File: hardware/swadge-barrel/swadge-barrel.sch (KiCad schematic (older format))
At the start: 44 parts, among them J1 USB_B_Micro, SW1 SW_SPDT, U1 AP1117-33, U2 ESP-13-WROOM-02D, U3 BUS_PCIexpress, U4 OLED_CONNECTOR, U5 QMA6981, U6 OLED_DISPLAY

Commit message: Updated descriptions to be more CSV friendly
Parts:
- U6: Notes Must be a single color, white. Must have SSD1306 driver. Mu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 -> Must be a single color; white. Must have SSD1306 driver. Mu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
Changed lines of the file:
@@
 F 6 "352" H 5850 6100 50  0001 C CNN "Cost100"
 F 7 "Y" H 5850 6100 50  0001 C CNN "Substitutable"
-F 8 "Must be a single color, white. Must have SSD1306 driver. Must have bottom pins, same as connector. 0.5mm pitch, like the connector" H 5850 6100 50  0001 C CNN "Notes"
+F 8 "Must be a single color; white. Must have SSD1306 driver. Must have bottom pins; same as connector. 0.5mm pitch; like the connector" H 5850 6100 50  0001 C CNN "Notes"
 	1    5850 6100
 	1    0    0    -1

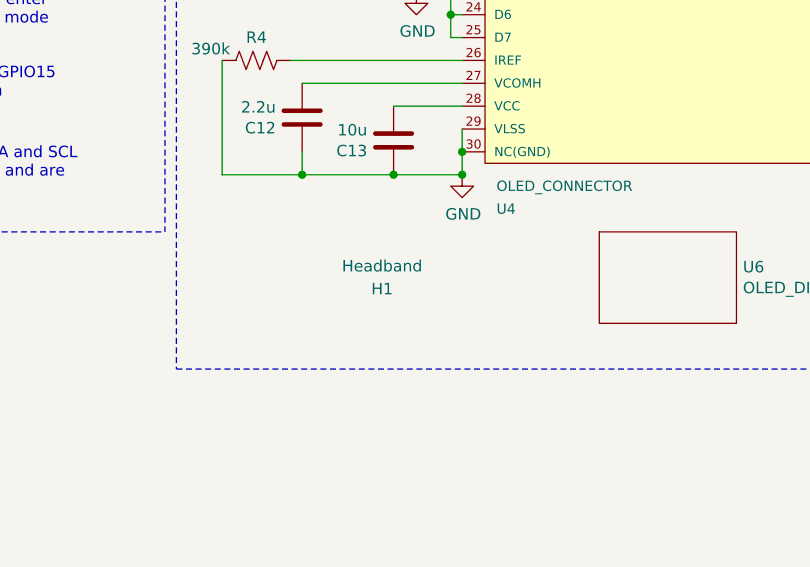
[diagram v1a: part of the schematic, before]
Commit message: Added H2 part designator
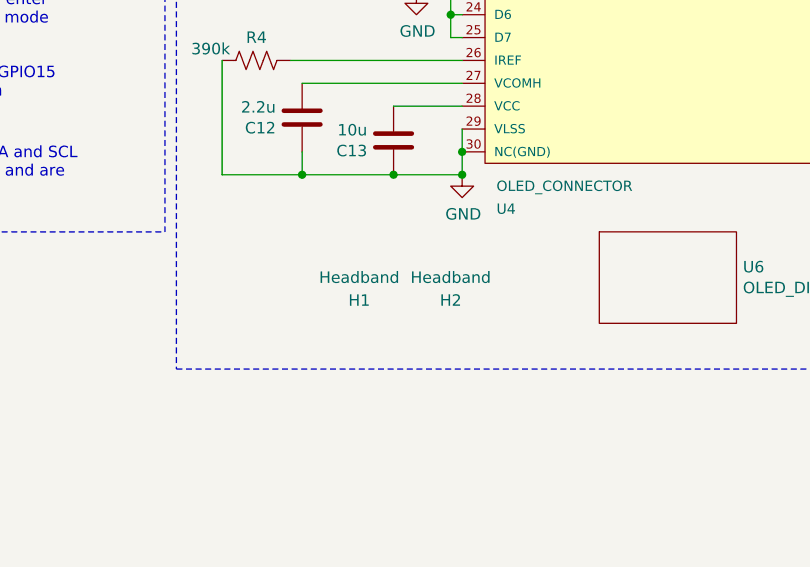
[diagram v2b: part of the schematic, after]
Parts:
- added H2: Headband, Swadge_Parts:NULL, symbol Swadge_Parts:Headband
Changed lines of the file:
@@
 L Swadge_Parts:Headband H1
 U 1 1 5D829692
-P 4600 6150
-F 0 "H1" H 4600 6150 50  0000 C CNN
-F 1 "Headband" H 4600 6250 50  0000 C CNN
-F 2 "Swadge_Parts:Headband" H 4600 6150 50  0001 C CNN
-F 3 "https://cdn.harwin.com/pdfs/M50-353.pdf" H 4600 6150 50  0001 C CNN
-F 4 "952-3598-ND" H 4600 6150 50  0001 C CNN "Digikey"
-F 5 "Use Swadge Headband PCB and two 2x1 male pin headers with 1.27mm spacing for assembly. Must attach OLED display before soldering headband. This is meant to protect the OLED's corners" H 4600 6150 50  0001 C CNN "Notes"
-F 6 "N" H 4600 6150 50  0001 C CNN "Substitutable"
-	1    4600 6150
+P 4500 6200
+F 0 "H1" H 4500 6200 50  0000 C CNN
+F 1 "Headband" H 4500 6300 50  0000 C CNN
+F 2 "Swadge_Parts:Headband" H 4500 6200 50  0001 C CNN
+F 3 "https://cdn.harwin.com/pdfs/M50-353.pdf" H 4500 6200 50  0001 C CNN
+F 4 "952-3598-ND" H 4500 6200 50  0001 C CNN "Digikey"
+F 5 "Use Swadge Headband PCB and two 2x1 male pin headers with 1.27mm spacing for assembly. Must attach OLED display before soldering headband. This is meant to protect the OLED's corners" H 4500 6200 50  0001 C CNN "Notes"
+F 6 "N" H 4500 6200 50  0001 C CNN "Substitutable"
+	1    4500 6200
 	1    0    0    -1
 $EndComp
@@
 Wire Notes Line
 	8550 2450 3700 2450
+$Comp
+L Swadge_Parts:Headband H2
+U 1 1 5DB44B4F
+P 4900 6200
+F 0 "H2" H 4900 6200 50  0000 C CNN
+F 1 "Headband" H 4900 6300 50  0000 C CNN
+F 2 "Swadge_Parts:NULL" H 4900 6200 50  0001 C CNN
+F 3 "https://cdn.harwin.com/pdfs/M50-353.pdf" H 4900 6200 50  0001 C CNN
+F 4 "952-3598-ND" H 4900 6200 50  0001 C CNN "Digikey"
+F 5 "This is the second 2x1 male pin header with 1.27mm spacing for assembly. " H 4900 6200 50  0001 C CNN "Notes"
+F 6 "N" H 4900 6200 50  0001 C CNN "Substitutable"
+	1    4900 6200
+	1    0    0    -1
+$EndComp
 $EndSCHEMATC

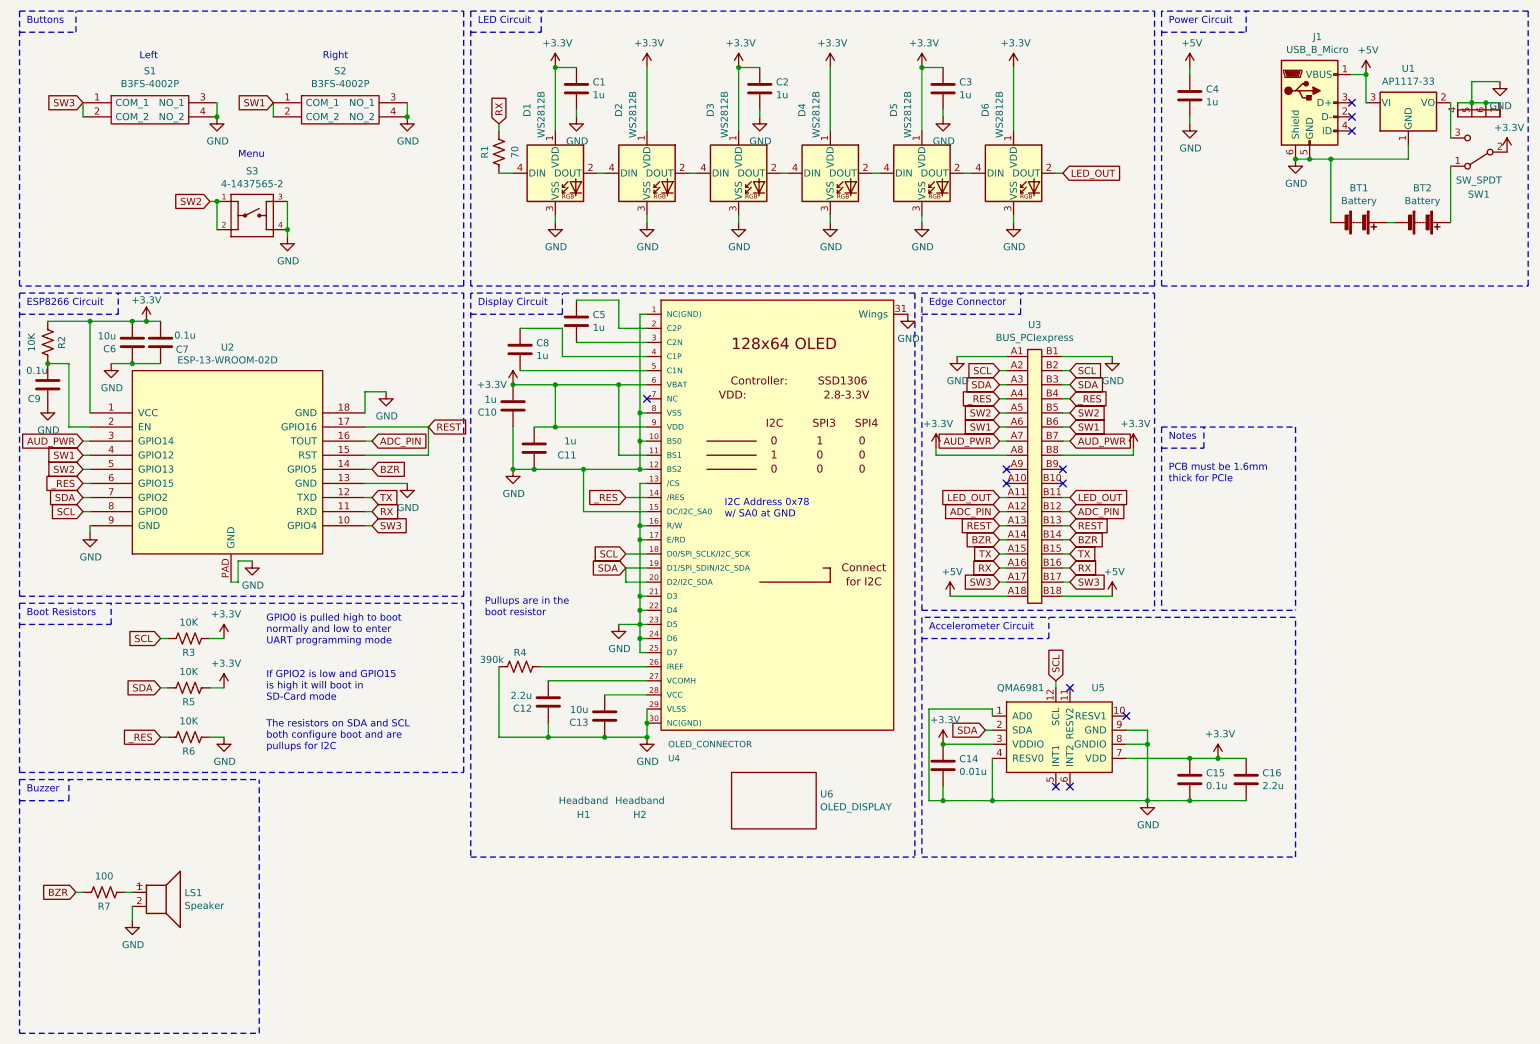
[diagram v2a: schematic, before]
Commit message: Modified barrel and programmer to use Swadge_Parts's power parts
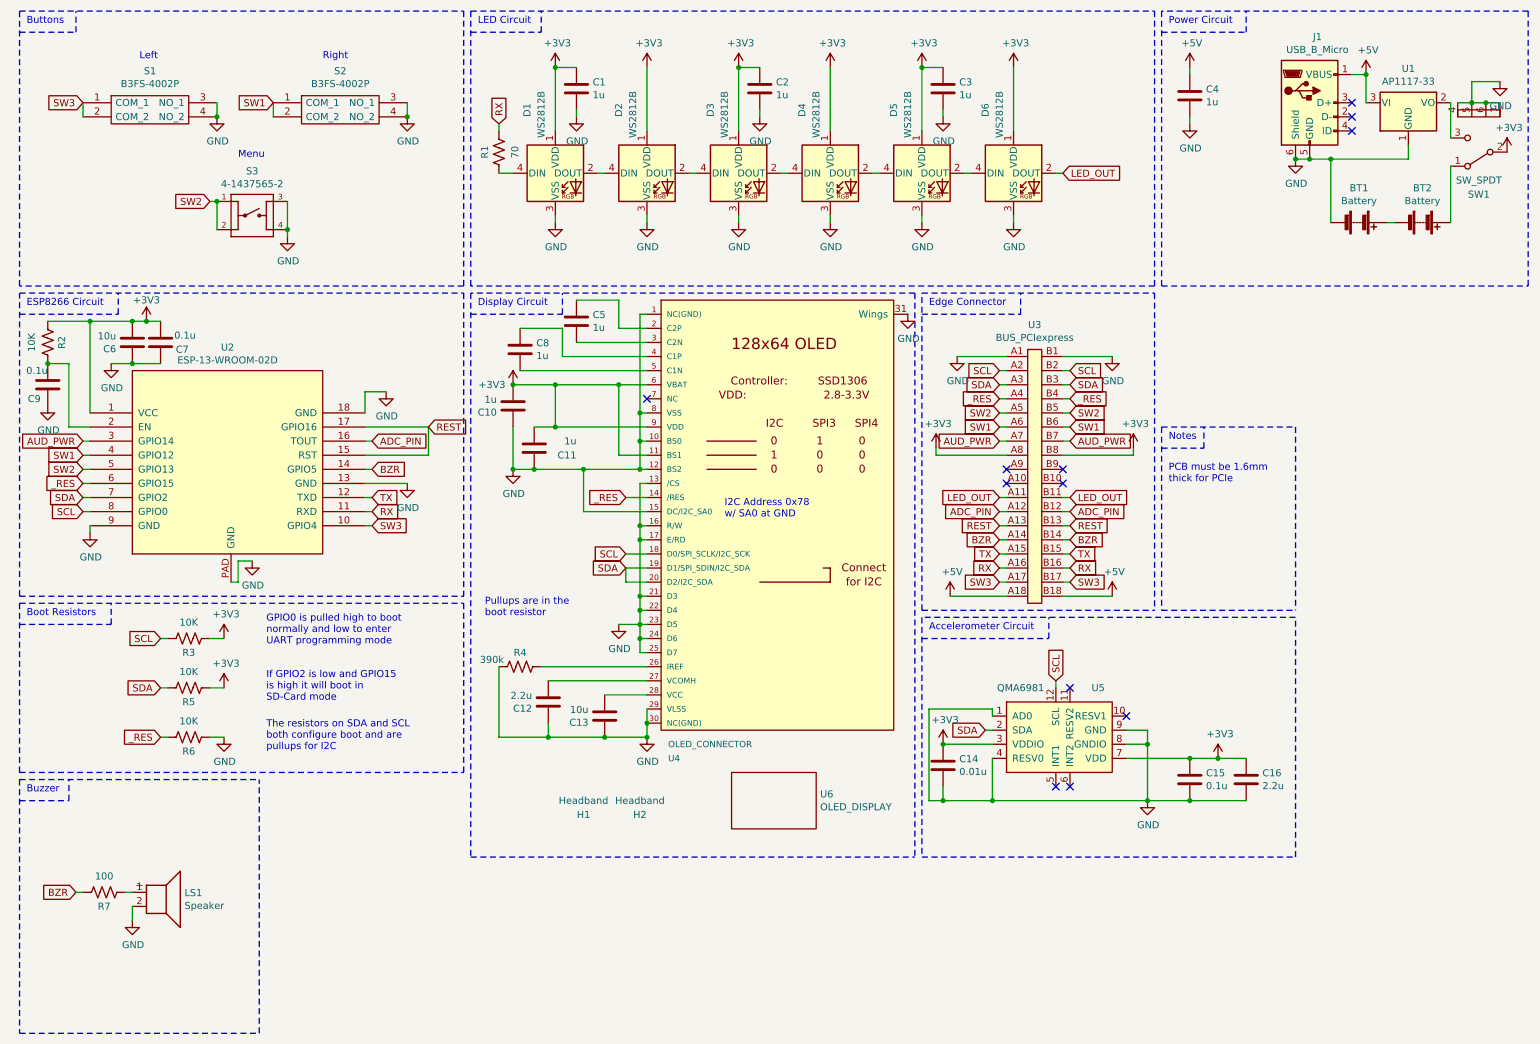
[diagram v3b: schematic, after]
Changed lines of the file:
@@
 $EndComp
 $Comp
-L power:+3.3V #PWR01
+L Swadge_Parts:+3V3 #PWR01
 U 1 1 5C3A6F38
 P 4300 900
 F 0 "#PWR01" H 4300 750 50  0001 C CNN
-F 1 "+3.3V" H 4315 1073 50  0000 C CNN
+F 1 "+3V3" H 4315 1073 50  0000 C CNN
 F 2 "" H 4300 900 50  0001 C CNN
 F 3 "" H 4300 900 50  0001 C CNN
@@
 $EndComp
 $Comp
-L power:GND #PWR012
+L Swadge_Parts:GND #PWR012
 U 1 1 5C3A6FCC
 P 4450 1250
@@
 Connection ~ 4300 900
 $Comp
-L power:GND #PWR018
+L Swadge_Parts:GND #PWR018
 U 1 1 5C3A78DA
 P 4300 2000
@@
 $EndComp
 $Comp
-L power:+3.3V #PWR02
+L Swadge_Parts:+3V3 #PWR02
 U 1 1 5C3A88AB
 P 4950 900
 F 0 "#PWR02" H 4950 750 50  0001 C CNN
-F 1 "+3.3V" H 4965 1073 50  0000 C CNN
+F 1 "+3V3" H 4965 1073 50  0000 C CNN
 F 2 "" H 4950 900 50  0001 C CNN
 F 3 "" H 4950 900 50  0001 C CNN
@@
 $EndComp
 $Comp
-L power:GND #PWR019
+L Swadge_Parts:GND #PWR019
 U 1 1 5C3A88C0
 P 4950 2000
@@
 $EndComp
 $Comp
-L power:+3.3V #PWR03
+L Swadge_Parts:+3V3 #PWR03
 U 1 1 5C3A91DF
 P 5600 900
 F 0 "#PWR03" H 5600 750 50  0001 C CNN
-F 1 "+3.3V" H 5615 1073 50  0000 C CNN
+F 1 "+3V3" H 5615 1073 50  0000 C CNN
 F 2 "" H 5600 900 50  0001 C CNN
 F 3 "" H 5600 900 50  0001 C CNN
@@
 $EndComp
 $Comp
-L power:GND #PWR013
+L Swadge_Parts:GND #PWR013
 U 1 1 5C3A91EB
 P 5750 1250
@@
 $EndComp
 $Comp
-L power:GND #PWR020
+L Swadge_Parts:GND #PWR020
 U 1 1 5C3A91F4
 P 5600 2000
@@
 $EndComp
 $Comp
-L power:+3.3V #PWR04
+L Swadge_Parts:+3V3 #PWR04
 U 1 1 5C3A9200
 P 6250 900
 F 0 "#PWR04" H 6250 750 50  0001 C CNN
-F 1 "+3.3V" H 6265 1073 50  0000 C CNN
+F 1 "+3V3" H 6265 1073 50  0000 C CNN
 F 2 "" H 6250 900 50  0001 C CNN
 F 3 "" H 6250 900 50  0001 C CNN
@@
 	6250 1350 6250 900
 $Comp
-L power:GND #PWR021
+L Swadge_Parts:GND #PWR021
 U 1 1 5C3A9215
 P 6250 2000
@@
 $EndComp
 $Comp
-L power:+3.3V #PWR05
+L Swadge_Parts:+3V3 #PWR05
 U 1 1 5C3A9722
 P 6900 900
 F 0 "#PWR05" H 6900 750 50  0001 C CNN
-F 1 "+3.3V" H 6915 1073 50  0000 C CNN
+F 1 "+3V3" H 6915 1073 50  0000 C CNN
 F 2 "" H 6900 900 50  0001 C CNN
 F 3 "" H 6900 900 50  0001 C CNN
@@
 $EndComp
 $Comp
-L power:GND #PWR014
+L Swadge_Parts:GND #PWR014
 U 1 1 5C3A972E
 P 7050 1250
@@
 Connection ~ 6900 900
 $Comp
-L power:GND #PWR022
+L Swadge_Parts:GND #PWR022
 U 1 1 5C3A9737
 P 6900 2000
@@
 $EndComp
 $Comp
-L power:+3.3V #PWR06
+L Swadge_Parts:+3V3 #PWR06
 U 1 1 5C3A9743
 P 7550 900
 F 0 "#PWR06" H 7550 750 50  0001 C CNN
-F 1 "+3.3V" H 7565 1073 50  0000 C CNN
+F 1 "+3V3" H 7565 1073 50  0000 C CNN
 F 2 "" H 7550 900 50  0001 C CNN
 F 3 "" H 7550 900 50  0001 C CNN
@@
 $EndComp
 $Comp
-L power:GND #PWR015
+L Swadge_Parts:GND #PWR015
 U 1 1 5C3A974F
 P 8800 1300
@@
 $EndComp
 $Comp
-L power:GND #PWR023
+L Swadge_Parts:GND #PWR023
 U 1 1 5C3A9758
 P 7550 2000
@@
 $EndComp
 $Comp
-L power:+3.3V #PWR042
+L Swadge_Parts:+3V3 #PWR042
 U 1 1 5C3B6E79
 P 1950 4950
 F 0 "#PWR042" H 1950 4800 50  0001 C CNN
-F 1 "+3.3V" H 1965 5123 50  0000 C CNN
+F 1 "+3V3" H 1965 5123 50  0000 C CNN
 F 2 "" H 1950 4950 50  0001 C CNN
 F 3 "" H 1950 4950 50  0001 C CNN
@@
 $EndComp
 $Comp
-L power:+3.3V #PWR043
+L Swadge_Parts:+3V3 #PWR043
 U 1 1 5C3B6EC6
 P 1950 5300
 F 0 "#PWR043" H 1950 5150 50  0001 C CNN
-F 1 "+3.3V" H 1965 5473 50  0000 C CNN
+F 1 "+3V3" H 1965 5473 50  0000 C CNN
 F 2 "" H 1950 5300 50  0001 C CNN
 F 3 "" H 1950 5300 50  0001 C CNN
@@
 $EndComp
 $Comp
-L power:GND #PWR044
+L Swadge_Parts:GND #PWR044
 U 1 1 5C3B6F13
 P 1950 5650
@@
 NoConn ~ 9950 1250
 $Comp
-L power:GND #PWR017
+L Swadge_Parts:GND #PWR017
 U 1 1 5C3F0918
 P 9550 1550
@@
 Connection ~ 9650 1550
 $Comp
-L power:+3.3V #PWR016
+L Swadge_Parts:+3V3 #PWR016
 U 1 1 5C40FB8F
 P 11050 1500
 F 0 "#PWR016" H 11050 1350 50  0001 C CNN
-F 1 "+3.3V" H 11065 1673 50  0000 C CNN
+F 1 "+3V3" H 11065 1673 50  0000 C CNN
 F 2 "" H 11050 1500 50  0001 C CNN
 F 3 "" H 11050 1500 50  0001 C CNN
@@
 SW1
 $Comp
-L power:GND #PWR024
+L Swadge_Parts:GND #PWR024
 U 1 1 5C4436EA
 P 2400 2100
@@
 	900  650  900  500
 $Comp
-L power:+5V #PWR08
+L Swadge_Parts:+5V #PWR08
 U 1 1 5C3BE999
 P 10050 950
@@
 $EndComp
 $Comp
-L power:+3.3V #PWR030
+L Swadge_Parts:+3V3 #PWR030
 U 1 1 5C437019
 P 4000 3150
 F 0 "#PWR030" H 4000 3000 50  0001 C CNN
-F 1 "+3.3V" H 3850 3150 50  0000 C CNN
+F 1 "+3V3" H 3850 3150 50  0000 C CNN
 F 2 "" H 4000 3150 50  0001 C CNN
 F 3 "" H 4000 3150 50  0001 C CNN
@@
 	4900 3750 4950 3750
 $Comp
-L power:GND #PWR035
+L Swadge_Parts:GND #PWR035
 U 1 1 5C478C8A
 P 4000 3750
@@
 Connection ~ 4250 5650
 $Comp
-L power:GND #PWR045
+L Swadge_Parts:GND #PWR045
 U 1 1 5C59A53E
 P 4950 5650
@@
 	4900 4150 4900 4250
 $Comp
-L power:GND #PWR041
+L Swadge_Parts:GND #PWR041
 U 1 1 5CCC3879
 P 4750 4850
@@
 SCL
 $Comp
-L power:GND #PWR037
+L Swadge_Parts:GND #PWR037
 U 1 1 5CD8FEC8
 P 1000 4200
@@
 $EndComp
 $Comp
-L power:+3.3V #PWR026
+L Swadge_Parts:+3V3 #PWR026
 U 1 1 5CD90854
 P 1400 2700
 F 0 "#PWR026" H 1400 2550 50  0001 C CNN
-F 1 "+3.3V" H 1400 2850 50  0000 C CNN
+F 1 "+3V3" H 1400 2850 50  0000 C CNN
 F 2 "" H 1400 2700 50  0001 C CNN
 F 3 "" H 1400 2700 50  0001 C CNN
@@
 	3400 3650 2950 3650
 $Comp
-L power:GND #PWR038
+L Swadge_Parts:GND #PWR038
 U 1 1 5CDDA877
 P 2150 4400
@@
 $EndComp
 $Comp
-L power:GND #PWR036
+L Swadge_Parts:GND #PWR036
 U 1 1 5CDDAE0D
 P 3250 3850
@@
 $EndComp
 $Comp
-L power:GND #PWR031
+L Swadge_Parts:GND #PWR031
 U 1 1 5CDDBB5A
 P 3100 3200
@@
 ADC_PIN
 $Comp
-L power:GND #PWR028
+L Swadge_Parts:GND #PWR028
 U 1 1 5CB24437
 P 8250 2950
@@
 $EndComp
 $Comp
-L power:+5V #PWR040
+L Swadge_Parts:+5V #PWR040
 U 1 1 5CB3C64C
 P 8250 4650
@@
 $EndComp
 $Comp
-L power:+3.3V #PWR034
+L Swadge_Parts:+3V3 #PWR034
 U 1 1 5CB52E95
 P 8400 3600
 F 0 "#PWR034" H 8400 3450 50  0001 C CNN
-F 1 "+3.3V" H 8415 3773 50  0000 C CNN
+F 1 "+3V3" H 8415 3773 50  0000 C CNN
 F 2 "" H 8400 3600 50  0001 C CNN
 F 3 "" H 8400 3600 50  0001 C CNN
@@
 AUD_PWR
 $Comp
-L power:+3.3V #PWR033
+L Swadge_Parts:+3V3 #PWR033
 U 1 1 5CCD0516
 P 7000 3600
 F 0 "#PWR033" H 7000 3450 50  0001 C CNN
-F 1 "+3.3V" H 7015 3773 50  0000 C CNN
+F 1 "+3V3" H 7015 3773 50  0000 C CNN
 F 2 "" H 7000 3600 50  0001 C CNN
 F 3 "" H 7000 3600 50  0001 C CNN
@@
 SW3
 $Comp
-L power:+5V #PWR039
+L Swadge_Parts:+5V #PWR039
 U 1 1 5CCD2242
 P 7100 4650
@@
 	7500 3050 7450 3050
 $Comp
-L power:GND #PWR027
+L Swadge_Parts:GND #PWR027
 U 1 1 5CDD49F2
 P 7150 2950
@@
 Connection ~ 700  3000
 $Comp
-L power:GND #PWR032
+L Swadge_Parts:GND #PWR032
 U 1 1 5D005F3B
 P 700 3300
@@
 	1500 3000 1300 3000
 $Comp
-L power:GND #PWR029
+L Swadge_Parts:GND #PWR029
 U 1 1 5D076E74
 P 1150 3000
@@
 NoConn ~ 7950 6000
 $Comp
-L power:GND #PWR048
+L Swadge_Parts:GND #PWR048
 U 1 1 5CE3B9AC
 P 8500 6100
@@
 	8500 5700 8500 6100
 $Comp
-L power:+3.3V #PWR046
+L Swadge_Parts:+3V3 #PWR046
 U 1 1 5CE6D6B7
 P 7050 5700
 F 0 "#PWR046" H 7050 5550 50  0001 C CNN
-F 1 "+3.3V" H 7065 5873 50  0000 C CNN
+F 1 "+3V3" H 7065 5873 50  0000 C CNN
 F 2 "" H 7050 5700 50  0001 C CNN
 F 3 "" H 7050 5700 50  0001 C CNN
@@
 Connection ~ 8500 6100
 $Comp
-L power:+3.3V #PWR047
+L Swadge_Parts:+3V3 #PWR047
 U 1 1 5CEBCCB3
 P 9000 5800
 F 0 "#PWR047" H 9000 5650 50  0001 C CNN
-F 1 "+3.3V" H 9015 5973 50  0000 C CNN
+F 1 "+3V3" H 9015 5973 50  0000 C CNN
 F 2 "" H 9000 5800 50  0001 C CNN
 F 3 "" H 9000 5800 50  0001 C CNN
@@
 	1900 1150 1900 1250
 $Comp
-L power:GND #PWR010
+L Swadge_Parts:GND #PWR010
 U 1 1 5D619825
 P 1900 1250
@@
 $EndComp
 $Comp
-L power:GND #PWR011
+L Swadge_Parts:GND #PWR011
 U 1 1 5C5BAFE0
 P 3250 1250
@@
 	1250 6750 1300 6750
 $Comp
-L power:GND #PWR049
+L Swadge_Parts:GND #PWR049
 U 1 1 5D5FD0B6
 P 1300 6950
@@
 	850  6100 850  5950
 $Comp
-L power:GND #PWR09
+L Swadge_Parts:GND #PWR09
 U 1 1 5D73519E
 P 11000 1000
@@
 Menu
 $Comp
-L power:GND #PWR025
+L Swadge_Parts:GND #PWR025
 U 1 1 5D809654
 P 6800 2650
@@
 	6850 2500 6850 6500
 $Comp
-L power:+5V #PWR07
+L Swadge_Parts:+5V #PWR07
 U 1 1 5DBABA5C
 P 8800 900

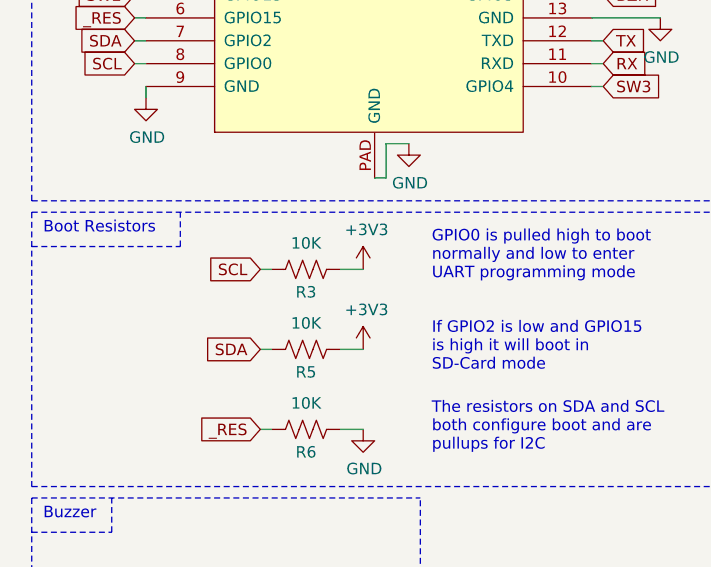
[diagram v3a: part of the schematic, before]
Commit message: Changed I2C pullups to 1K Updated digikey part numbers on BOM
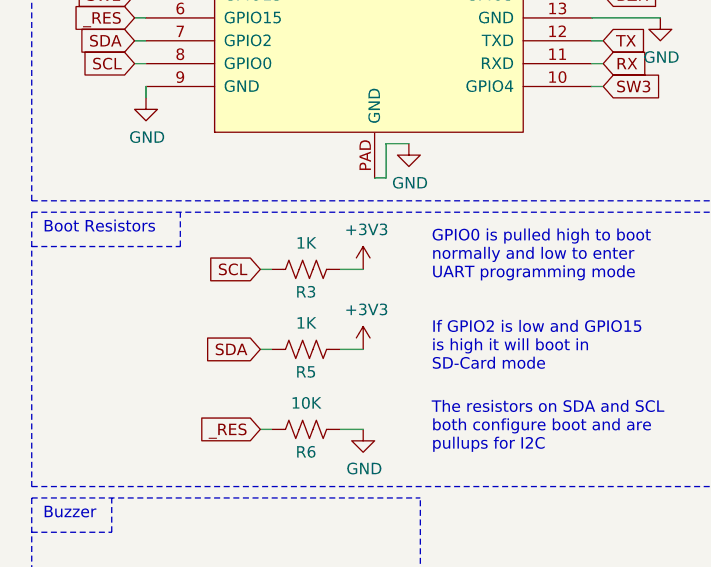
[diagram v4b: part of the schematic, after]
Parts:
- C14: Digikey 1276-1000-1-ND -> 1292-1622-2-ND
- R3, R5: value 10K -> 1K; Digikey RNCP0603FTD10K0CT-ND -> 2037-PFR05S-102-FNHTR-ND
- R7: Digikey RNCP0603FTD10K0CT-ND -> 311-100JRTR-ND
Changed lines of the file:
@@
 EESchema Schematic File Version 4
 LIBS:swadge-barrel-cache
-EELAYER 29 0
+EELAYER 30 0
 EELAYER END
 $Descr A4 11693 8268
@@
 P 1700 4950
 F 0 "R3" V 1800 4950 50  0000 C CNN
-F 1 "10K" V 1586 4950 50  0000 C CNN
+F 1 "1K" V 1586 4950 50  0000 C CNN
 F 2 "Swadge_Parts:R_0603_1608Metric" V 1740 4940 50  0001 C CNN
 F 3 "" H 1700 4950 50  0001 C CNN
 F 4 "10" H 0   0   50  0001 C CNN "Cost100"
-F 5 "RNCP0603FTD10K0CT-ND" H 0   0   50  0001 C CNN "Digikey"
+F 5 "2037-PFR05S-102-FNHTR-ND" H 0   0   50  0001 C CNN "Digikey"
 F 6 "Y" H 0   0   50  0001 C CNN "Substitutable"
 F 7 "0603 Package" H 1700 4950 50  0001 C CNN "Notes"
@@
 P 1700 5300
 F 0 "R5" V 1800 5300 50  0000 C CNN
-F 1 "10K" V 1586 5300 50  0000 C CNN
+F 1 "1K" V 1586 5300 50  0000 C CNN
 F 2 "Swadge_Parts:R_0603_1608Metric" V 1740 5290 50  0001 C CNN
 F 3 "" H 1700 5300 50  0001 C CNN
 F 4 "10" H 0   0   50  0001 C CNN "Cost100"
-F 5 "RNCP0603FTD10K0CT-ND" H 0   0   50  0001 C CNN "Digikey"
+F 5 "2037-PFR05S-102-FNHTR-ND" H 0   0   50  0001 C CNN "Digikey"
 F 6 "Y" H 0   0   50  0001 C CNN "Substitutable"
 F 7 "0603 Package" H 1700 5300 50  0001 C CNN "Notes"
@@
 F 3 "" H 7050 5850 50  0001 C CNN
 F 4 "10" H 4200 -1100 50  0001 C CNN "Cost100"
-F 5 "1276-1000-1-ND" H 4200 -1100 50  0001 C CNN "Digikey"
+F 5 "1292-1622-2-ND" H 4200 -1100 50  0001 C CNN "Digikey"
 F 6 "Y" H 4200 -1100 50  0001 C CNN "Substitutable"
 F 7 "0603 Package" H 7050 5850 50  0001 C CNN "Notes"
@@
 F 3 "" H 1100 6750 50  0001 C CNN
 F 4 "10" H -600 1100 50  0001 C CNN "Cost100"
-F 5 "RNCP0603FTD10K0CT-ND" H -600 1100 50  0001 C CNN "Digikey"
+F 5 "311-100JRTR-ND" H -600 1100 50  0001 C CNN "Digikey"
 F 6 "Y" H -600 1100 50  0001 C CNN "Substitutable"
 F 7 "0603 Package" H 1100 6750 50  0001 C CNN "Notes"
